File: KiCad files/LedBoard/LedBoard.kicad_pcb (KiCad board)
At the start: 2 copper layers, 40 x 40 mm, 18 parts, among them J1 Conn_01x02, J2 Conn_01x02, J3 Conn_01x02, Q1 IRLR120NTRPBF

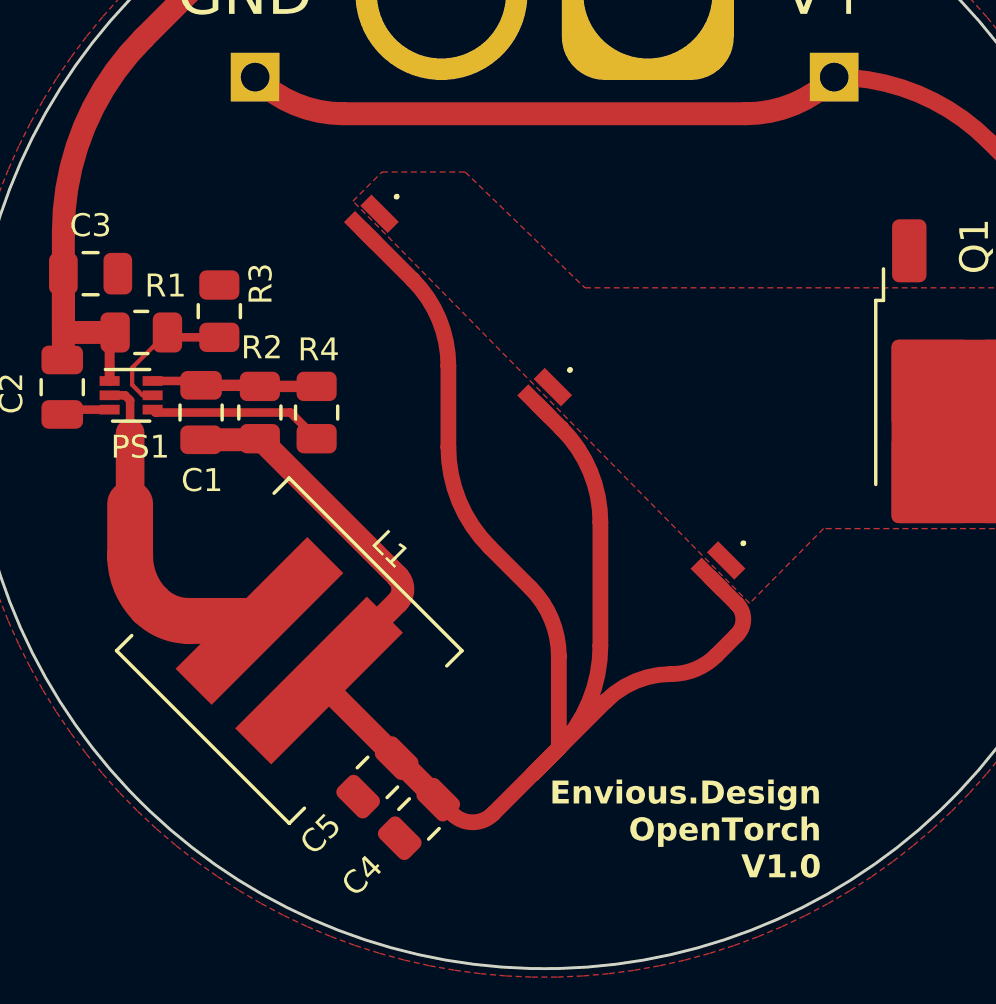
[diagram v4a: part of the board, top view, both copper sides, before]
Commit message: replaced traces with zones
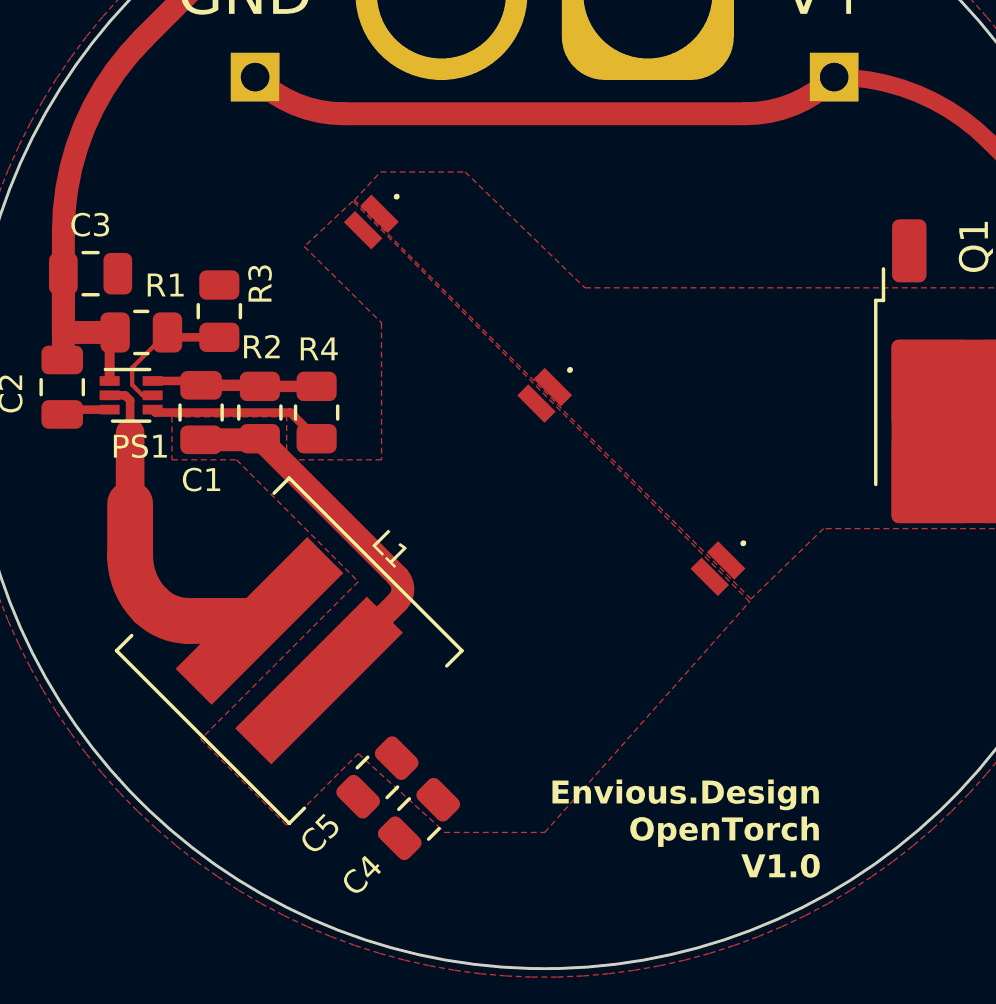
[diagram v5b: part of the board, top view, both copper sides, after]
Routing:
- net LED_V+: track 72.6 -> 15.7 mm
- added copper zone on F.Cu, net LED_V+
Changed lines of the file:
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@@
     )
   )
-  (segment (start 86.287689 51.10678) (end 86.782664 51.601755) (width 0.55) (layer "F.Cu") (net 1))
-  (segment (start 90.494975 49.303658) (end 90.494975 46.107465) (width 0.55) (layer "F.Cu") (net 1))
-  (segment (start 96.709209 44.281965) (end 95.759385 43.332141) (width 0.55) (layer "F.Cu") (net 1))
   (segment (start 78.052039 38.513541) (end 80.06515 38.513541) (width 0.4) (layer "F.Cu") (net 1))
-  (segment (start 89.713622 37.286378) (end 90.590921 38.163678) (width 0.55) (layer "F.Cu") (net 1))
-  (segment (start 91.944544 45.732769) (end 91.944544 41.431611) (width 0.55) (layer "F.Cu") (net 1))
-  (segment (start 95.988656 46.072719) (end 96.709209 45.352166) (width 0.55) (layer "F.Cu") (net 1))
   (segment (start 82.129902 46.948992) (end 84.866876 44.212018) (width 0.8) (layer "F.Cu") (net 1))
-  (segment (start 89.893934 49.904699) (end 90.444544 49.354089) (width 0.55) (layer "F.Cu") (net 1))
   (segment (start 80.102649 38.55104) (end 84.866876 43.315268) (width 0.8) (layer "F.Cu") (net 1))
-  (segment (start 89.611091 50.187541) (end 90.494975 49.303658) (width 0.55) (layer "F.Cu") (net 1))
-  (segment (start 89.505025 43.717514) (end 88.091242 42.303731) (width 0.55) (layer "F.Cu") (net 1))
-  (segment (start 84.83812 49.657211) (end 86.287689 51.10678) (width 0.8) (layer "F.Cu") (net 1))
-  (segment (start 89.893934 49.904699) (end 92.125915 47.672718) (width 0.55) (layer "F.Cu") (net 1))
-  (segment (start 89.611091 50.187541) (end 89.893934 49.904699) (width 0.55) (layer "F.Cu") (net 1))
   (segment (start 78.01454 38.55104) (end 80.102649 38.55104) (width 0.8) (layer "F.Cu") (net 1))
   (segment (start 78.01454 38.55104) (end 78.052039 38.513541) (width 0.4) (layer "F.Cu") (net 1))
-  (segment (start 83.667859 31.240615) (end 85.396243 32.969) (width 0.55) (layer "F.Cu") (net 1))
-  (segment (start 86.641243 38.803122) (end 86.641243 35.974695) (width 0.55) (layer "F.Cu") (net 1))
-  (segment (start 88.196878 51.601755) (end 89.611091 50.187541) (width 0.55) (layer "F.Cu") (net 1))
-  (segment (start 82.129902 46.948992) (end 84.83812 49.657211) (width 0.8) (layer "F.Cu") (net 1))
-  (arc (start 92.125915 47.672718) (mid 93.178183 46.969615) (end 94.419417 46.722718) (width 0.55) (layer "F.Cu") (net 1))
-  (arc (start 91.944544 41.431611) (mid 91.592749 39.663019) (end 90.590921 38.163678) (width 0.55) (layer "F.Cu") (net 1))
-  (arc (start 90.444544 49.354089) (mid 91.554706 47.692613) (end 91.944544 45.732769) (width 0.55) (layer "F.Cu") (net 1))
-  (arc (start 86.782664 51.601755) (mid 87.489771 51.894649) (end 88.196878 51.601755) (width 0.55) (layer "F.Cu") (net 1))
-  (arc (start 94.419417 46.722718) (mid 95.268683 46.55379) (end 95.988656 46.072719) (width 0.55) (layer "F.Cu") (net 1))
-  (arc (start 96.709209 45.352166) (mid 96.930854 44.817065) (end 96.709209 44.281965) (width 0.55) (layer "F.Cu") (net 1))
   (arc (start 84.866876 44.212018) (mid 85.052599 43.763643) (end 84.866876 43.315268) (width 0.8) (layer "F.Cu") (net 1))
-  (arc (start 90.494975 46.107465) (mid 90.237696 44.814033) (end 89.505025 43.717514) (width 0.55) (layer "F.Cu") (net 1))
-  (arc (start 85.396243 32.969) (mid 86.317678 34.348024) (end 86.641243 35.974695) (width 0.55) (layer "F.Cu") (net 1))
-  (arc (start 88.091242 42.303731) (mid 87.018085 40.697638) (end 86.641243 38.803122) (width 0.55) (layer "F.Cu") (net 1))
   (segment (start 76.325022 36.500001) (end 77.863499 36.500001) (width 0.3) (layer "F.Cu") (net 2))
   (segment (start 80.06515 36.688541) (end 80.02765 36.651041) (width 0.4) (layer "F.Cu") (net 2))
@@
     )
   )
+  (zone (net 1) (net_name "LED_V+") (layer "F.Cu") (hatch edge 0.5)
+    (priority 1)
+    (connect_pads yes (clearance 0.15))
+    (min_thickness 0.25) (filled_areas_thickness no)
+    (fill yes (thermal_gap 0.15) (thermal_bridge_width 0.25) (smoothing fillet) (radius 1))
+    (polygon
+      (pts
+        (xy 86.5 52.25)
+        (xy 90 52.25)
+        (xy 97.15 44.2)
+        (xy 83.312 30.226)
+        (xy 81.613793 31.809383)
+        (xy 84.308592 34.47179)
+        (xy 84.31 39.25)
+        (xy 81 39.25)
+        (xy 81 37.75)
+        (xy 77 37.75)
+        (xy 77 39.25)
+        (xy 79.25 39.25)
+        (xy 83.5 43.5)
+        (xy 78 49)
+        (xy 81 52)
+        (xy 83.5 49.5)
+        (xy 86.25 52)
+      )
+    )
+  )
   (zone (net 8) (net_name "NPN_DRAIN") (layer "F.Cu") (hatch edge 0.5)
     (priority 2)
-    (connect_pads (clearance 0.15))
+    (connect_pads yes (clearance 0.15))
     (min_thickness 0.15) (filled_areas_thickness no)
     (fill yes (thermal_gap 0.5) (thermal_bridge_width 1) (smoothing fillet) (radius 1))
@@
         (xy 108.05 41.65)
         (xy 99.729307 41.65)
-        (xy 97.149424 44.258002)
-        (xy 83.312 30.226)
-        (xy 84.328 29.21)
+        (xy 97.199424 44.108002)
+        (xy 83.364914 30.193848)
+        (xy 84.273081 29.21)
         (xy 87.226514 29.21)
       )

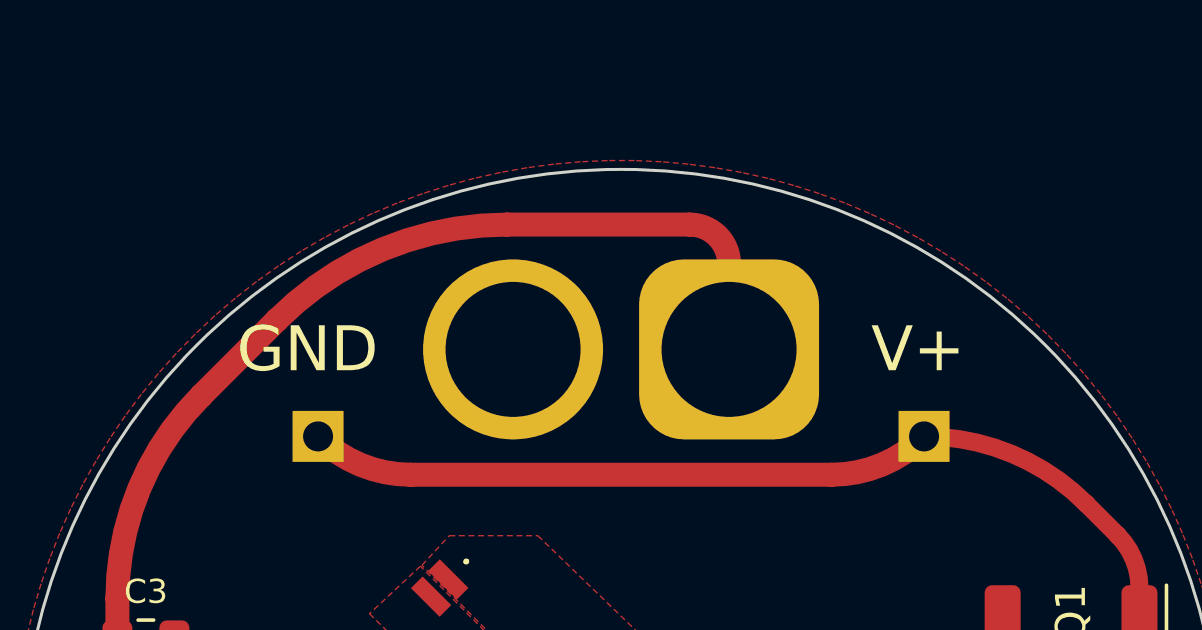
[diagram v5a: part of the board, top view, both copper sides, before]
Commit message: corrected VCC and GND being swapped
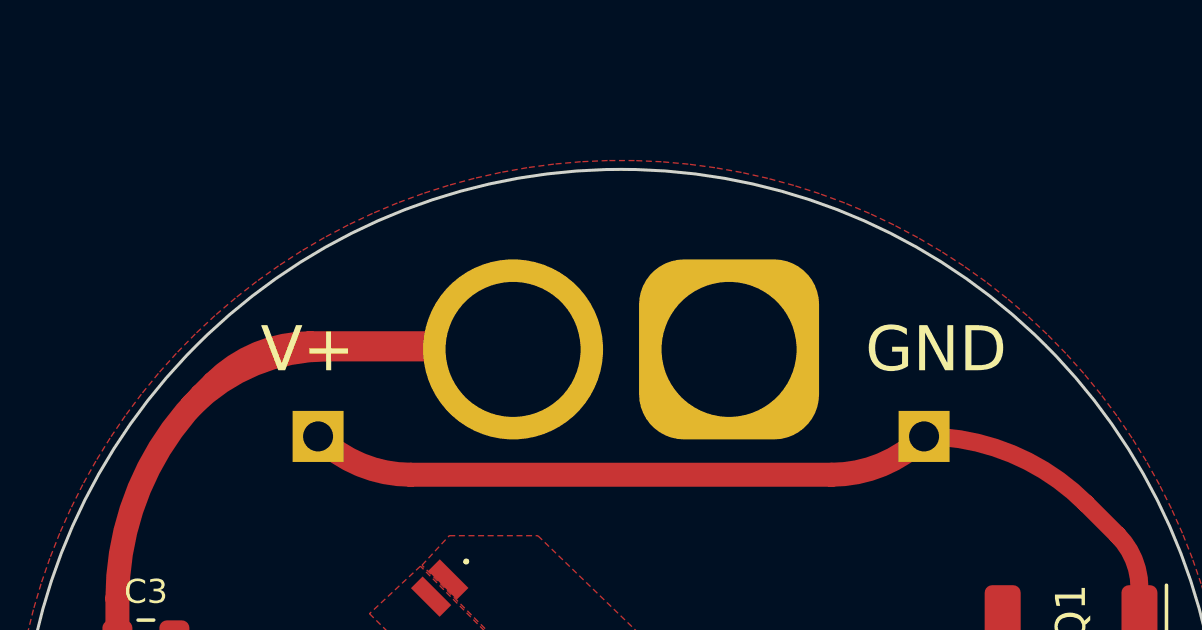
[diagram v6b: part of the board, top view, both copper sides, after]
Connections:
- J1 pad 1: VCC -> GND
- J1 pad 2: GND -> VCC
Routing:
- net VCC: track 40.6 -> 39.7 mm
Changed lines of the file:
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@@
       (stroke (width 0.12) (type solid)) (layer "B.Fab"))
     (pad "1" thru_hole roundrect (at 0 0 180) (size 6 6) (drill 4.5) (layers "*.Cu" "*.Mask") (roundrect_rratio 0.25)
-      (net 4 "VCC") (pinfunction "Pin_1") (pintype "passive"))
+      (net 3 "GND") (pinfunction "Pin_1") (pintype "passive"))
     (pad "2" thru_hole circle (at 7.2 0 180) (size 6 6) (drill 4.5) (layers "*.Cu" "*.Mask")
-      (net 3 "GND") (pinfunction "Pin_2") (pintype "passive"))
+      (net 4 "VCC") (pinfunction "Pin_2") (pintype "passive"))
     (model "${KICAD6_3DMODEL_DIR}/Connector_AMASS.3dshapes/AMASS_XT60-F_1x02_P7.2mm_Vertical.wrl"
       (offset (xyz 0 0 0))
       (scale (xyz 1 1 1))
       (rotate (xyz 0 0 0))
+    )
+    (model "C:/Users/Envy/Documents/GitHub/EnvOpenTorch/KiCad files/IOController/IOController.step"
+      (offset (xyz 3.6 -6.2 51.4))
+      (scale (xyz 1 1 1))
+      (rotate (xyz 90 0 0))
     )
   )
@@
   (gr_circle (center 90 37) (end 110 37)
     (stroke (width 0.1) (type default)) (fill none) (layer "Edge.Cuts"))
-  (gr_text "V+" (at 99.9 23) (layer "F.SilkS")
+  (gr_text "V+" (at 79.55 23) (layer "F.SilkS")
     (effects (font (size 1.5 1.5) (thickness 0.25)))
   )
@@
     (effects (font (size 0.8 0.8) (thickness 0.153) bold) (justify right top))
   )
-  (gr_text "GND" (at 79.55 23) (layer "F.SilkS")
+  (gr_text "GND" (at 100.5 23) (layer "F.SilkS")
     (effects (font (size 1.5 1.5) (thickness 0.25)))
   )
@@
   (segment (start 76.325022 37.499999) (end 76.426063 37.601041) (width 0.3) (layer "F.Cu") (net 3))
   (segment (start 81.132549 37.601041) (end 82.045049 38.513541) (width 0.3) (layer "F.Cu") (net 3))
-  (segment (start 93.599999 23) (end 93.599999 20.15219) (width 0.8) (layer "F.Cu") (net 4))
-  (segment (start 78.537233 22.012767) (end 76.011523 24.538477) (width 0.8) (layer "F.Cu") (net 4))
-  (segment (start 92.286554 18.838745) (end 86.2 18.838745) (width 0.8) (layer "F.Cu") (net 4))
+  (segment (start 86.399999 23) (end 80.206549 23) (width 0.8) (layer "F.Cu") (net 4))
   (segment (start 73.170859 35.767158) (end 73.210809 35.727208) (width 0.8) (layer "F.Cu") (net 4))
   (segment (start 73.210808 31.3) (end 73.210808 32.757359) (width 0.8) (layer "F.Cu") (net 4))
   (segment (start 74.825022 36.500001) (end 74.825022 34.999022) (width 0.35) (layer "F.Cu") (net 4))
   (segment (start 73.210809 35.727208) (end 73.210809 32.757359) (width 0.8) (layer "F.Cu") (net 4))
+  (segment (start 79.630979 22.794111) (end 85.902939 22.794111) (width 0.8) (layer "F.Cu") (net 4))
   (segment (start 73.210809 34.807969) (end 73.210809 32.757359) (width 0.8) (layer "F.Cu") (net 4))
+  (segment (start 76.43 24.12) (end 76.011523 24.538477) (width 0.8) (layer "F.Cu") (net 4))
   (segment (start 74.825022 34.999022) (end 75.016075 34.807969) (width 0.35) (layer "F.Cu") (net 4))
   (segment (start 73.170859 35.767158) (end 73.170859 35.727208) (width 0.35) (layer "F.Cu") (net 4))
   (segment (start 75.016075 34.807969) (end 73.210809 34.807969) (width 0.8) (layer "F.Cu") (net 4))
   (arc (start 76.011523 24.538477) (mid 73.93869 27.640689) (end 73.210808 31.3) (width 0.8) (layer "F.Cu") (net 4))
-  (arc (start 93.599999 20.15219) (mid 93.2153 19.223444) (end 92.286554 18.838745) (width 0.8) (layer "F.Cu") (net 4))
-  (arc (start 86.2 18.838745) (mid 82.05294 19.663646) (end 78.537233 22.012767) (width 0.8) (layer "F.Cu") (net 4))
+  (arc (start 80.206549 23) (mid 77.76635 23.485385) (end 75.697648 24.867648) (width 0.8) (layer "F.Cu") (net 4))
+  (arc (start 76.43 24.12) (mid 77.898621 23.138699) (end 79.630979 22.794111) (width 0.8) (layer "F.Cu") (net 4))
+  (arc (start 85.902939 22.794111) (mid 86.171945 22.84762) (end 86.399999 23) (width 0.8) (layer "F.Cu") (net 4))
   (segment (start 75.539666 40.783021) (end 75.539666 42.611448) (width 1.6) (layer "F.Cu") (net 5))
   (segment (start 77.578317 44.870098) (end 80.051008 44.870098) (width 1.6) (layer "F.Cu") (net 5))

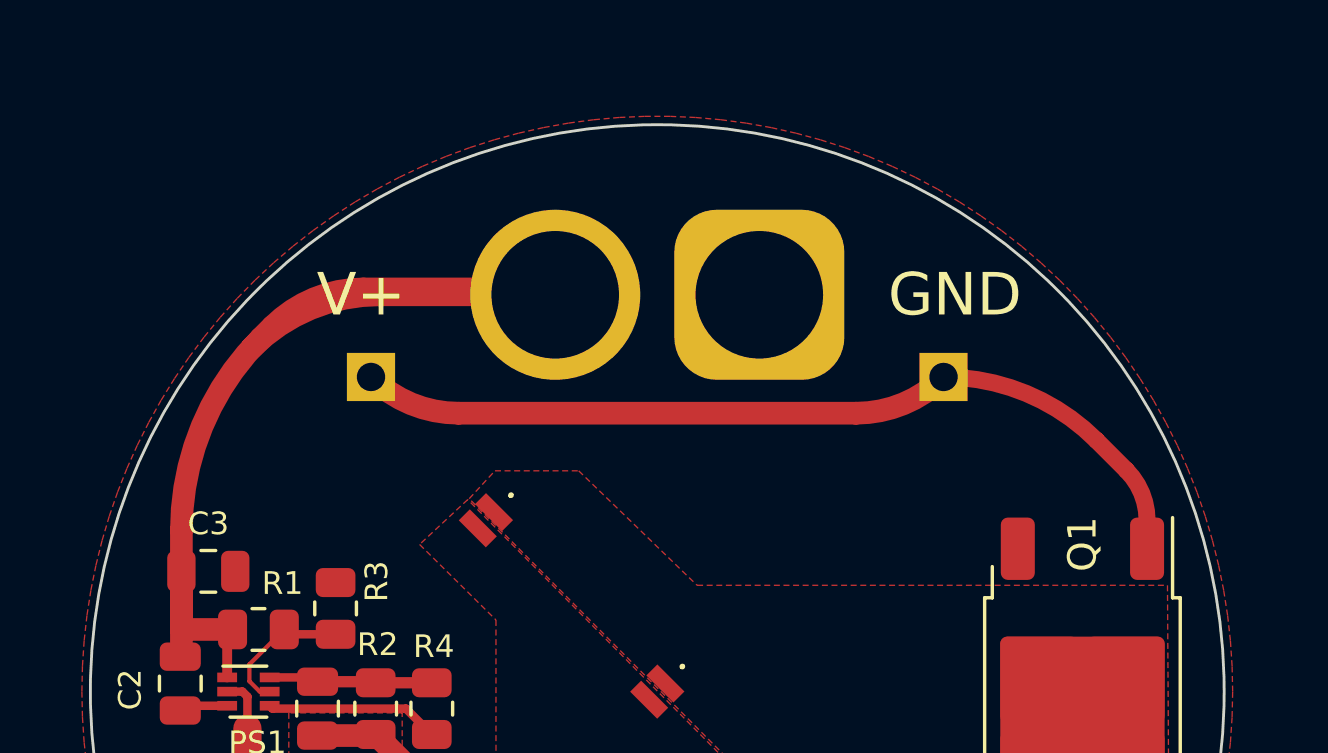
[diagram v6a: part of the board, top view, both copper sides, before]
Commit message: changed an XT60 to edge connector because I didnt like the XT60 and pin header setup.
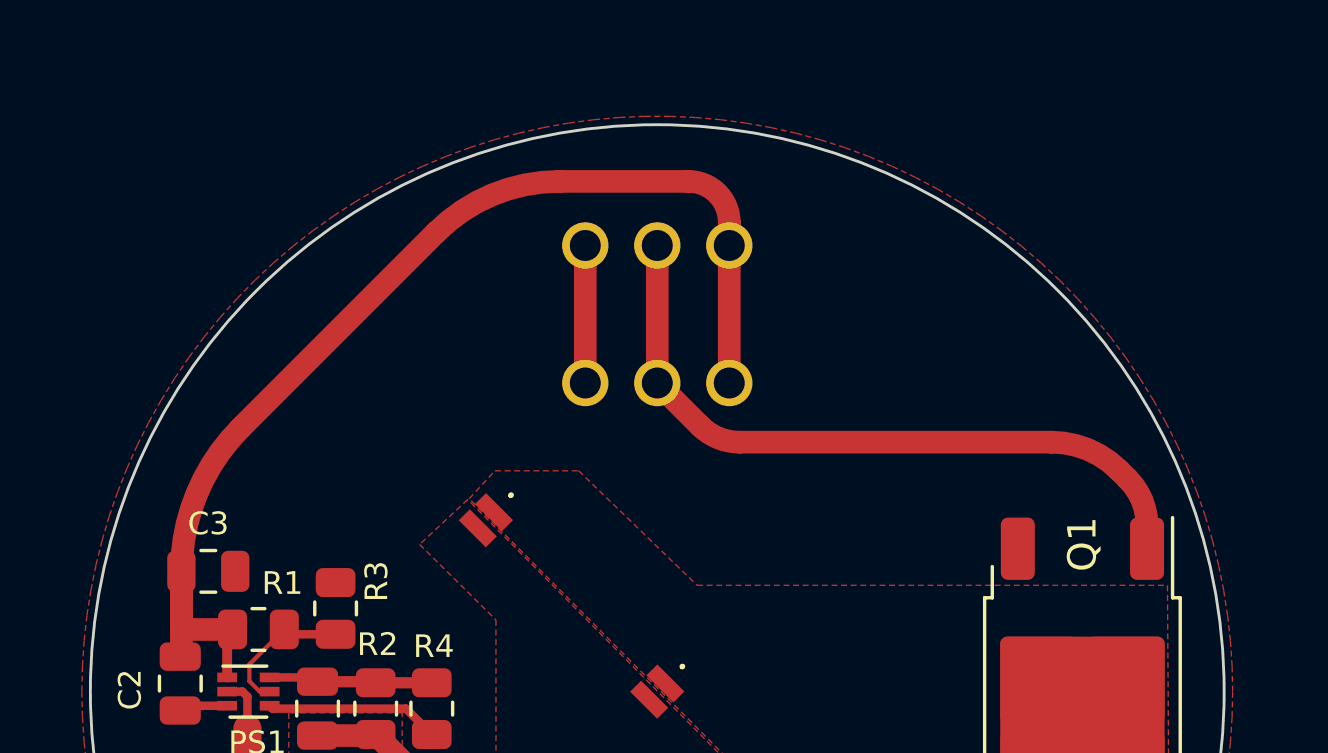
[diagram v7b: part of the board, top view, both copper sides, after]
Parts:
- removed J1: Conn_01x02, Connector_AMASS:AMASS_XT60-F_1x02_P7.20mm_Vertical
- removed J2, J3: Conn_01x02, Connector_PinSocket_2.54mm:PinSocket_1x01_P2.54mm_Vertical
- added J4: 7-5530843-7, 7-5530843-7:755308437, B.Cu at (92.5, 26.1)
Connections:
- Q1 pad 1: Net-(J2-Pin_1) -> NPN GATE
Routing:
- net Net-(J2-Pin_1): track 31.2 -> 0.00 mm
- net NPN GATE: track 0.00 -> 25.2 mm
- net GND: track 7.86 -> 12.7 mm
- net VCC: track 39.7 -> 41.3 mm
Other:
- board text removed: "GND"
- board text removed: "V+"

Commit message: added footprints for some discontinued LEDs i have spare of, added level shifter to ensure gate voltage is above threshold
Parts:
- added LEDB1: GW VJLPL1.CM-K3LX-XX55-1, GWVJLPL1CMK3LXXX511:GWVJLPL1CMK3LXXX511, F.Cu at (94.0, 41.0)
- added LEDB3: GW VJLPL1.CM-K3LX-XX55-1, GWVJLPL1CMK3LXXX511:GWVJLPL1CMK3LXXX511, F.Cu at (86.0, 33.0)
- LED1, LED2, LED3: footprint GWVJLPL1CMK3LXXX511:GWVJLPL1CMK3LXXX511 -> GW_VJLPE1:GW_VJLPE1.CM_0.91x0.91mm
- turned LED1 to -45 degrees
- turned LED2 to -45 degrees
- turned LED3 to -45 degrees
